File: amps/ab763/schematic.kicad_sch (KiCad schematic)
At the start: 114 parts, among them T1 125P33A, T2 125C3A, T3 125A1A, T4 125A20B

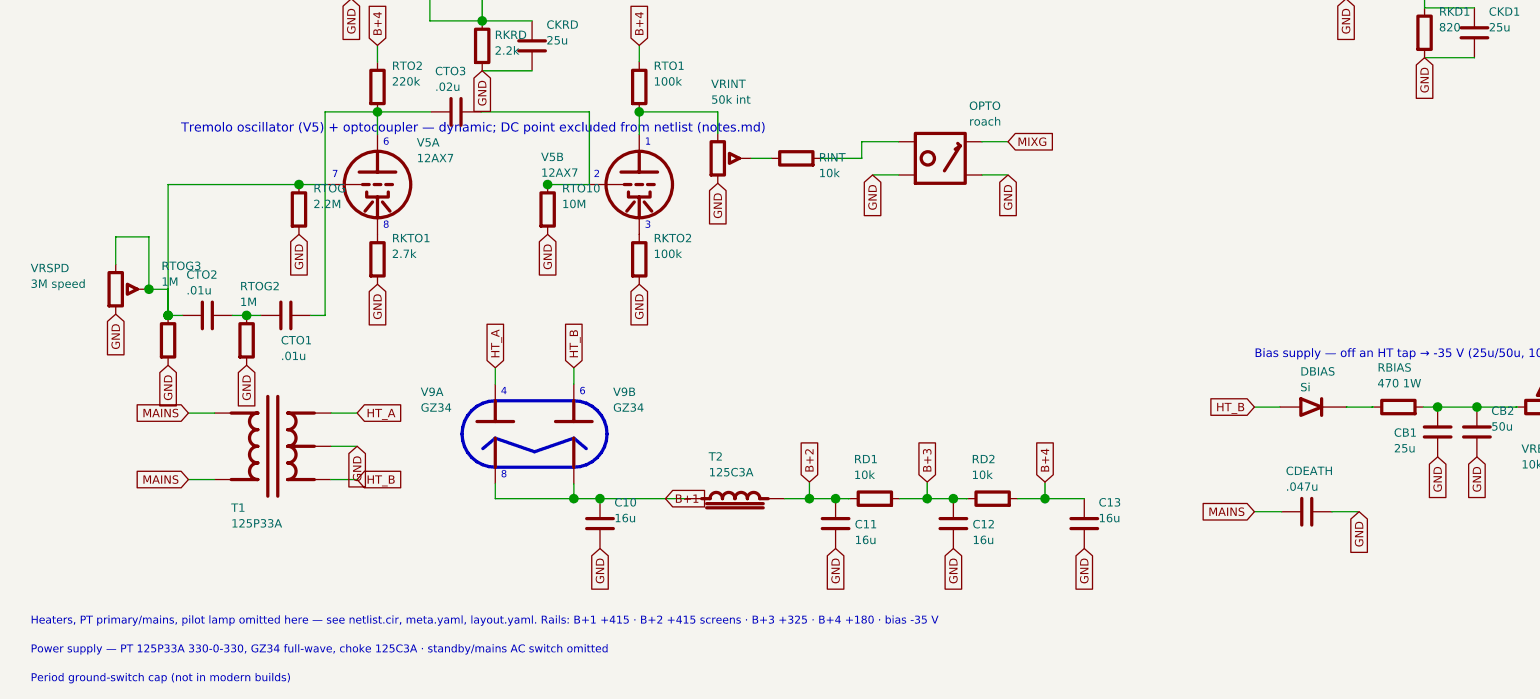
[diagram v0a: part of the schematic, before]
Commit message: Fix: schematic sheet notes no longer name repository files
Thirty-seven committed sheets rendered footnotes and section notes such as
"Heaters and PT primary omitted — see netlist.cir and meta.yaml" or
"excluded from netlist.cir (notes.md)" to visitors through KiCanvas. The
prose sweeps never counted sheets. Rewritten in the site's own words — the
netlist, the sources list, the circuit story, the parts list, the board
drawing — in 59 strings across 33 draw scripts, keeping every technical
claim as it was; the three tone sheets (6G4, 6G5, 6G6-B) are under repair
elsewhere and keep theirs for now. The sweep touched only strings passed to
the sheet's note, text, caption and footnote calls, never a path or a value.

Gates: check_schematics 40/0, connectivity 0 isolated pins;
verify_schematic_nets 40 clean; only the regenerated sheets and their served
copies changed.

Co-Authored-By: Claude Fable 5.1 <noreply@anthropic.com>
Claude-Session: https://claude.ai/code/session_01KBMfdh37HmCL2iWcBiL5J1
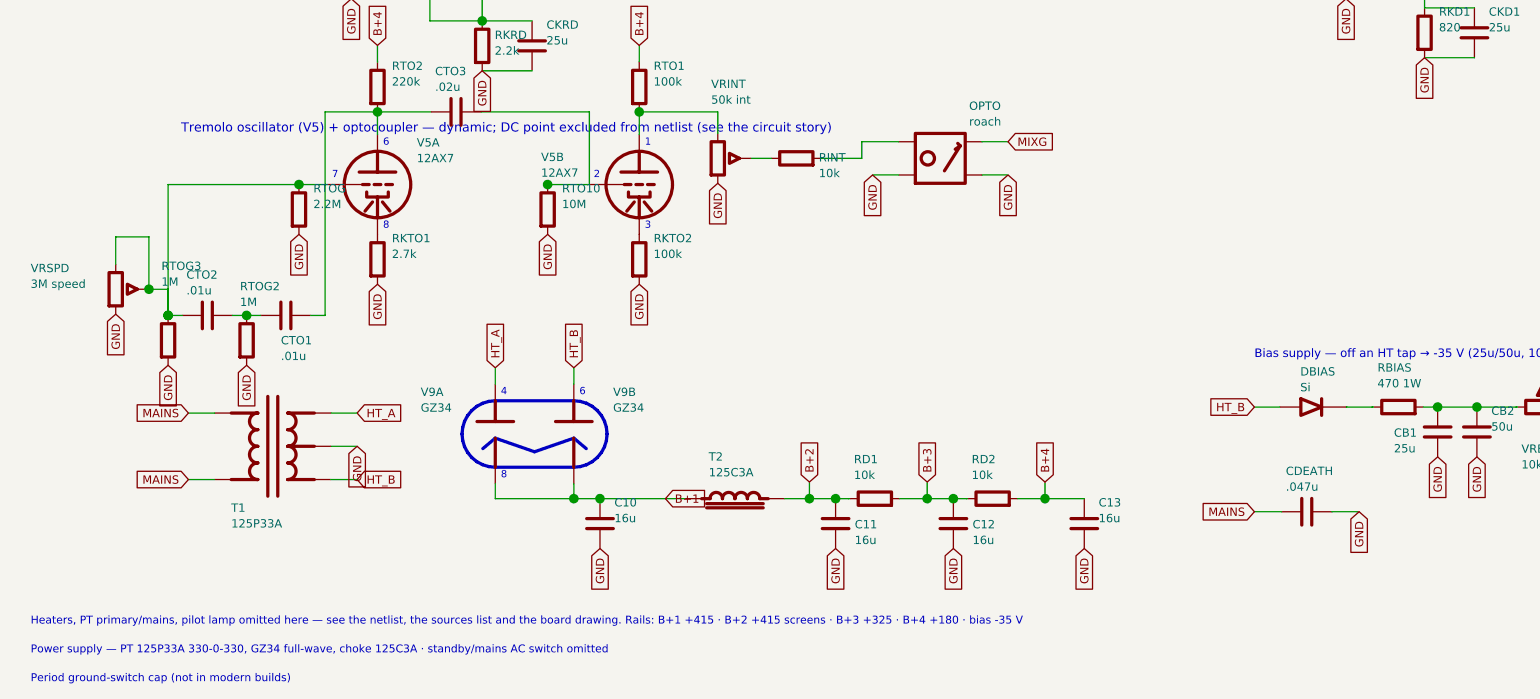
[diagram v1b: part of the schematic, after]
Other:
- note added: "Heaters, PT primary/mains, pilot lamp omitted here — see the netlist, the sources list and the board drawing. Rails: B+1 +415 · B+2 +415 screens · B+3 +325 · B+4 +180 · bias -35 V"
- note added: "Tremolo oscillator (V5) + optocoupler — dynamic; DC point excluded from netlist (see the circuit story)"
- note removed: "Heaters, PT primary/mains, pilot lamp omitted here — see netlist.cir, meta.yaml, layout.yaml. Rails: B+1 +415 · B+2 +415 screens · B+3 +325 · B+4 +180 · bias -35 V"
- note removed: "Tremolo oscillator (V5) + optocoupler — dynamic; DC point excluded from netlist (notes.md)"
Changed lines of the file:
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@@
   (global_label "PIG" (shape input) (at 241.7 130.278 0)
     (effects (font (size 1.27 1.27)) (justify left)))
-  (text "Tremolo oscillator (V5) + optocoupler — dynamic; DC point excluded from netlist (notes.md)" (at 35.7 177.778 0)
+  (text "Tremolo oscillator (V5) + optocoupler — dynamic; DC point excluded from netlist (see the circuit story)" (at 35.7 177.778 0)
     (effects (font (size 1.4 1.4)) (justify left)))
   (symbol (lib_id "cx:TRIODE") (at 65.7 186.278 0) (unit 1)
@@
   (text "6" (at 96.55 218.048 0)
     (effects (font (size 1.1 1.1)) (justify left)))
-  (text "Heaters, PT primary/mains, pilot lamp omitted here — see netlist.cir, meta.yaml, layout.yaml. Rails: B+1 +415 · B+2 +415 screens · B+3 +325 · B+4 +180 · bias -35 V" (at 12.7 253.056 0)
+  (text "Heaters, PT primary/mains, pilot lamp omitted here — see the netlist, the sources list and the board drawing. Rails: B+1 +415 · B+2 +415 screens · B+3 +325 · B+4 +180 · bias -35 V" (at 12.7 253.056 0)
     (effects (font (size 1.2 1.2)) (justify left)))
   (text "Power supply — PT 125P33A 330-0-330, GZ34 full-wave, choke 125C3A · standby/mains AC switch omitted" (at 12.7 257.456 0)

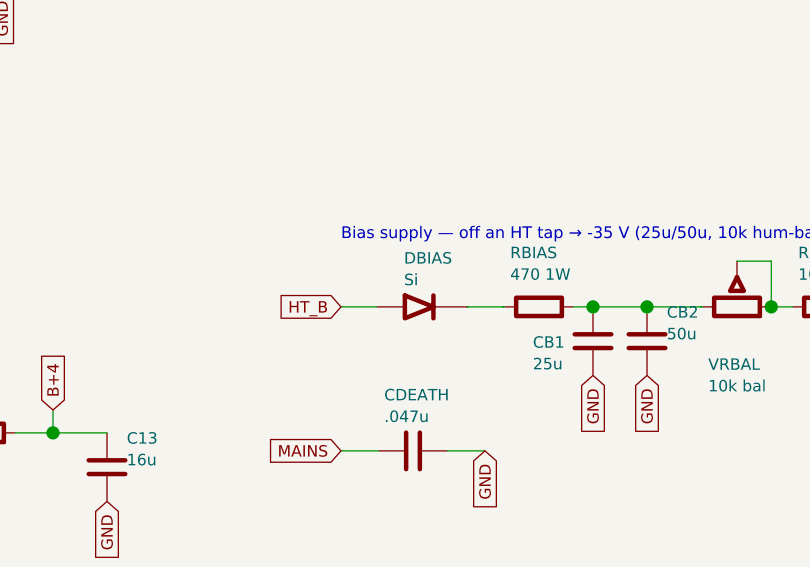
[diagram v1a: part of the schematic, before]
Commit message: Fix: 17 bias rectifiers and six HT diodes drawn backwards; the 6G6-B and 6G4 bias rows as their drawings show; AA1164 V4 units
Rectifier polarity has no gate. The netlists model every supply as an ideal
source, the sheet-vs-board check treats a two-terminal part as unordered, and
the boards' `cathode:` fields were copied from the sheets. Measured over all
68 diodes on 40 sheets: 18 negative-bias rectifiers had the cathode on the
negative node (a diode that way round would charge the node POSITIVE), and all
six 6G6-B HT diodes pointed away from B+. The printed negative bias on each of
those sheets falsifies the drawn orientation; the nine bias rectifiers already
right (AA1164, AA864, AB165, B15N, DR103, JTM100, M1959, M2204, 6G6-B) show
the idiom. Flipped: 5E4-A, 5E5-A, 5E6-A, 5F10, 5F4, 5F6, 5F6-A, 5F8-A, 5G9,
6G2, 6G3, 6G4, 6G5, AA964, AB763, AB763 Super, AB763 Twin, JTM45 (the
M1987's is with the Marshall board repair) and the 6G6-B's DR1-DR6. The
5F8-A board, which had copied its sheet, has the band moved to the tap side;
the other boards' bands are with the board-repair wave. A gate is next.

6G6-B bias. E-FB (6431x3364): the 1K 1W rises from TR1's SECOND secondary
terminal, a bias tap between the upper HT end and the grounded centre tap,
to the diode's + end. The sheet fed the diode from the HT end with the 1K
after it. T1 now carries its tap pin and the row reads tap -> 1K -> diode ->
-54 V. (The triage had read "HT end"; the native crop shows the tap.)

6G4 bias. A-FJ, read natively: tap -> rectifier -> 8 uF -> 10K -> the -55 V
node, which carries a second 8 uF and the 56K to ground as a bleeder. The
sheet fed the rectifier from an HT end, drew the 56K in series and carried
one capacitor. CBIAS2 joins the parts list, and RBIAS1's role now says
bleeder.

AA1164 V4. The K-FD sheet prints the phase inverter 7/6/8 and the tremolo
oscillator 2/1/3 (5554x4346); the sheet had them the other way round.

Gates: check_schematics 40/0 (+selftest), verify_schematic_nets 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
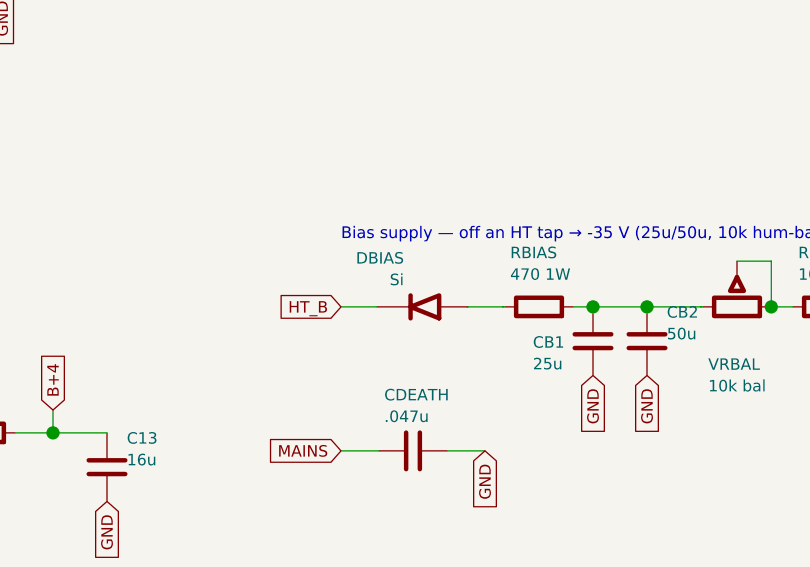
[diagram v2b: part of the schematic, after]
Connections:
- net HT_B: now also DBIAS.2 (K); no longer DBIAS.1 (A)
- net at RBIAS.1: now also DBIAS.1 (A); no longer DBIAS.2 (K)
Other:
- moved on the sheet: DBIAS
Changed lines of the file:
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@@
   (wire (pts (xy 199.7 220.278) (xy 203.62 220.278))
     (stroke (width 0) (type default)))
-  (symbol (lib_id "cx:DIODE_SS") (at 208.7 220.278 0) (unit 1)
+  (symbol (lib_id "cx:DIODE_SS") (at 208.7 220.278 180) (unit 1)
     (in_bom yes) (on_board yes)
     (property "Reference" "DBIAS" (at 206.7 214.878 0) (effects (font (size 1.27 1.27)) (justify left)))

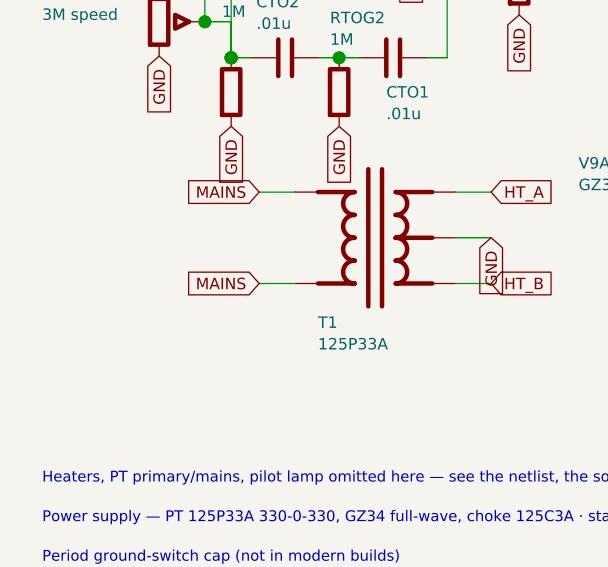
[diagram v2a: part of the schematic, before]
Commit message: Fix: the 6G5's rectifier was connected to nothing; 17 sheets shorted the mains by naming both leads alike
6G5 power supply. The sheet drew four diodes as a "silicon bridge" whose
HT_A/HT_B labels stopped 6 mm short of their wires. D1/D2's anodes sat on
the tremolo's cathode node (a tremolo wire's end touched the old diode
stub), D3/D4 ran from ground to the reservoir, and TR1's centre tap floated
under an open-pin waiver whose stated reason was the bridge itself.
A-FJ (Schematic Heaven 2153x1437, read enlarged): each HT end of TR1 runs
through a leg of three silicon diodes, every + (cathode) toward the +460 V
reservoir; the centre tap is grounded; TR1's second secondary terminal is a
bias tap feeding the 6G4's network part for part: rectifier, 8-150, 10K,
then 8-150 and a 56K bleeder at the -55 V line. Redrawn as the drawing
shows: D1-D6, TR1 with its tap pin, the centre tap to ground, the bias
network (CBIAS 25 uF -> 8 uF; RBIAS2, CBIAS2, RBIAS1 added), the waiver
deleted, and the notes, meta, netlist header and parts list no longer say
bridge. Not yet carried: the drawing's second 20-600 at the reservoir and
the standby switch (this sheet omits chassis switches by its own note);
and the tremolo ladder still runs through the transformer's corner of the
sheet, a layout clash rather than a connection, queued for its own redraw.

Mains. Two global labels with one name are one net. 16 of 24 power
transformers on the sheets carried a label named MAINS on both primary
leads, so the winding's two pins were one net: 5E4-A, 5E5-A, 5F4, 5G9,
6161, 6G2, 6G3, 6G4, AA1164, AA764, AA764-Vibro, AA964, AB763, AB763
Super, AB763 Twin, GA-40. The 6G5's loop ran from one MAINS label through
switch, fuse and winding back to the same name. No gate models the primary,
so a copy-pasted idiom did this. The second lead is now MAINS N, the AC15's
idiom; the AA1164's and AA964's second AC row, drawn under the first row's
name, is the neutral. The death and across-the-line caps stay on the le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
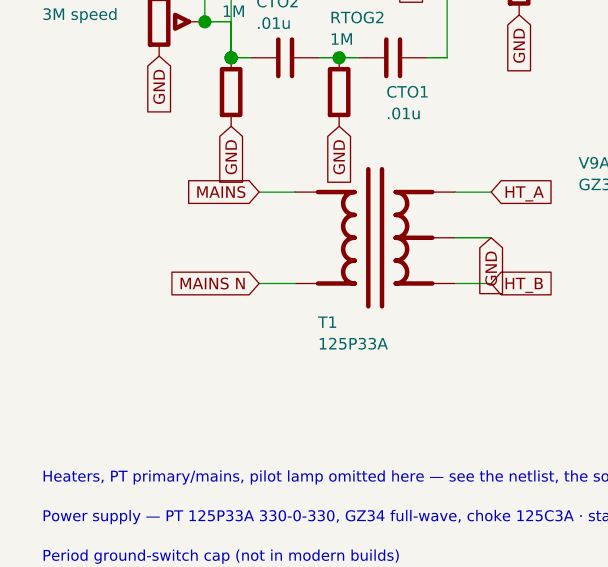
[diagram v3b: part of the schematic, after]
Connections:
- net MAINS: no longer T1.2 (PRI_2)
- new net MAINS N: T1.2 (PRI_2)
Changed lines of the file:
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@@
   (wire (pts (xy 40.81 231.358) (xy 36.81 231.358))
     (stroke (width 0) (type default)))
-  (global_label "MAINS" (shape input) (at 36.81 231.358 180)
+  (global_label "MAINS N" (shape input) (at 36.81 231.358 180)
     (effects (font (size 1.27 1.27)) (justify right)))
   (wire (pts (xy 58.59 221.198) (xy 62.59 221.198))
